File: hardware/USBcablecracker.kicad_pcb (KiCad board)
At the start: 2 copper layers, 100 x 50 mm, 55 parts, among them P1 USB_A, P10 USB_A, P11 USB_B, P2 CONN_01X02, P3 USB_B-Micro, P7 USB_B-Mini, P8 USB_B-Micro-3.0, P9 USB_TYPEC-S, SW1 Switch_SPDT_x2, U1 ATmega32U4-AU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

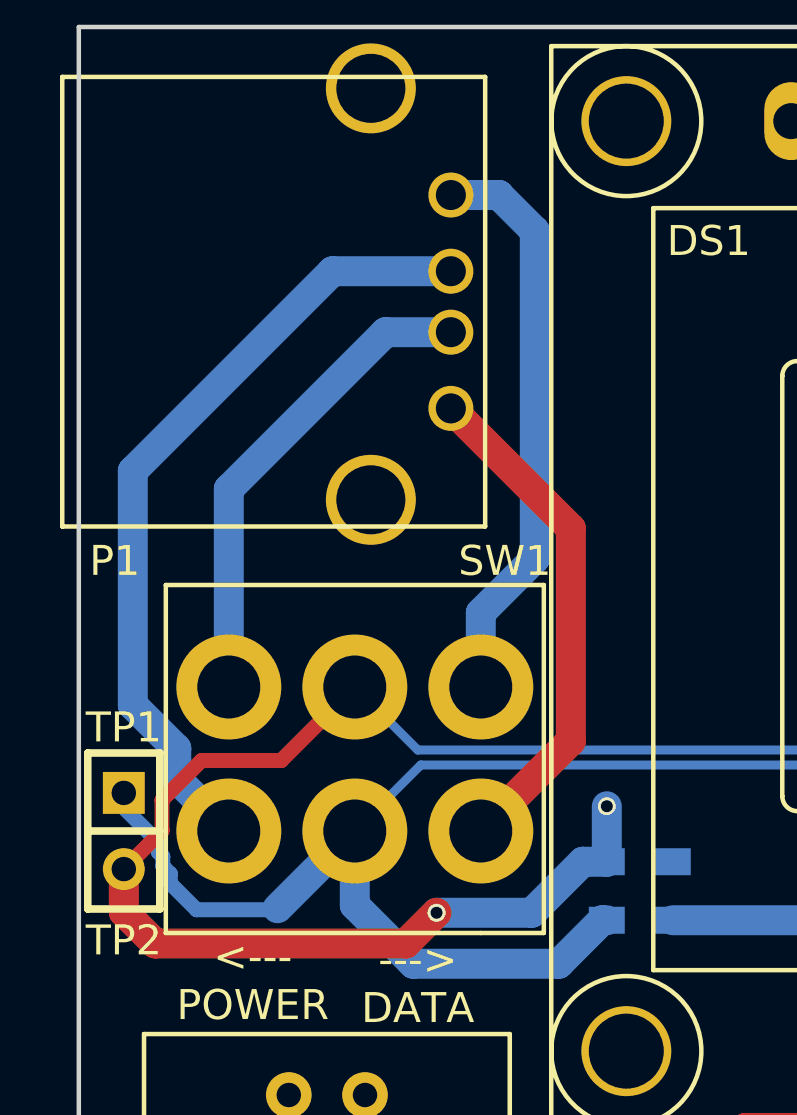
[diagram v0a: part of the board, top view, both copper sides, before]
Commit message: replacing switch by pin headers for easy sourcing
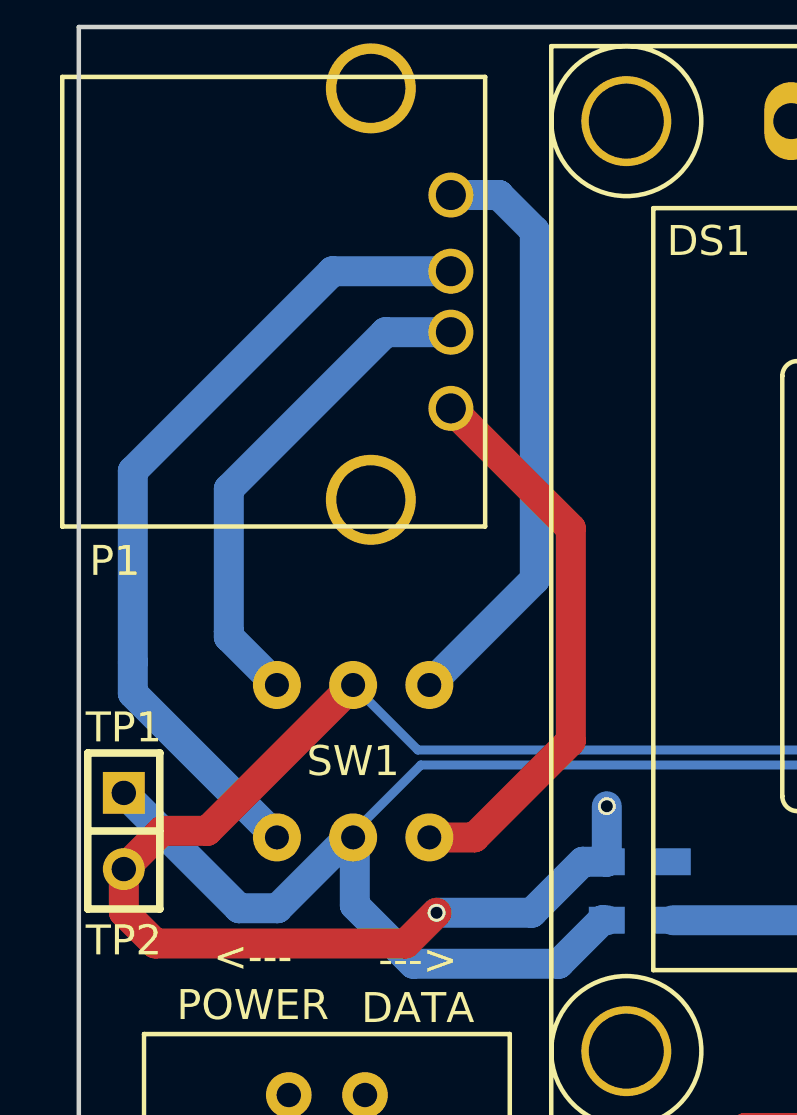
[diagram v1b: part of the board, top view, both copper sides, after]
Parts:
- SW1: footprint USBcablecracker:DPDT -> USBcablecracker:pin_headers_switch
- moved SW1 4.85 mm to (59.1, 74.5), turned to 0 degrees
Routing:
- net /TP2: track 90.8 -> 93.2 mm
- net Net-(P1-Pad4): track 17.0 -> 18.8 mm
- net /TP1: track 79.8 -> 78.8 mm
- net Net-(P1-Pad2): track 26.7 -> 27.6 mm
- net Net-(P1-Pad1): track 19.2 -> 19.9 mm
- net Net-(P1-Pad3): track 16.2 -> 16.8 mm

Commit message: reverted to original switch
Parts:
- SW1: footprint USBcablecracker:pin_headers_switch -> USBcablecracker:DPDT
- moved SW1 4.85 mm to (63.4, 76.8), turned to 90 degrees
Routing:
- net /TP2: track 93.2 -> 90.8 mm
- net Net-(P1-Pad4): track 18.8 -> 17.0 mm
- net /TP1: track 78.8 -> 79.8 mm
- net Net-(P1-Pad2): track 27.6 -> 26.7 mm
- net Net-(P1-Pad1): track 19.9 -> 19.2 mm
- net Net-(P1-Pad3): track 16.8 -> 16.2 mm
